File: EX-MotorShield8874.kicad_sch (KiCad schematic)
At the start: 23 parts, among them J101 MC 1,5/ 2-G-3,5, J101 Power, J102 Analog, J103 Digital/PWM, J103 MC 1,5/ 2-G-3,5, J104 Digital/PWM, J105 STEMMA QT, J106 I2C, J107 OLED, J108 USB_B_Micro, J111 JTAG, SW101 FLASH, U101 ESP32-S2-MINI-2, Y101 40Mhz

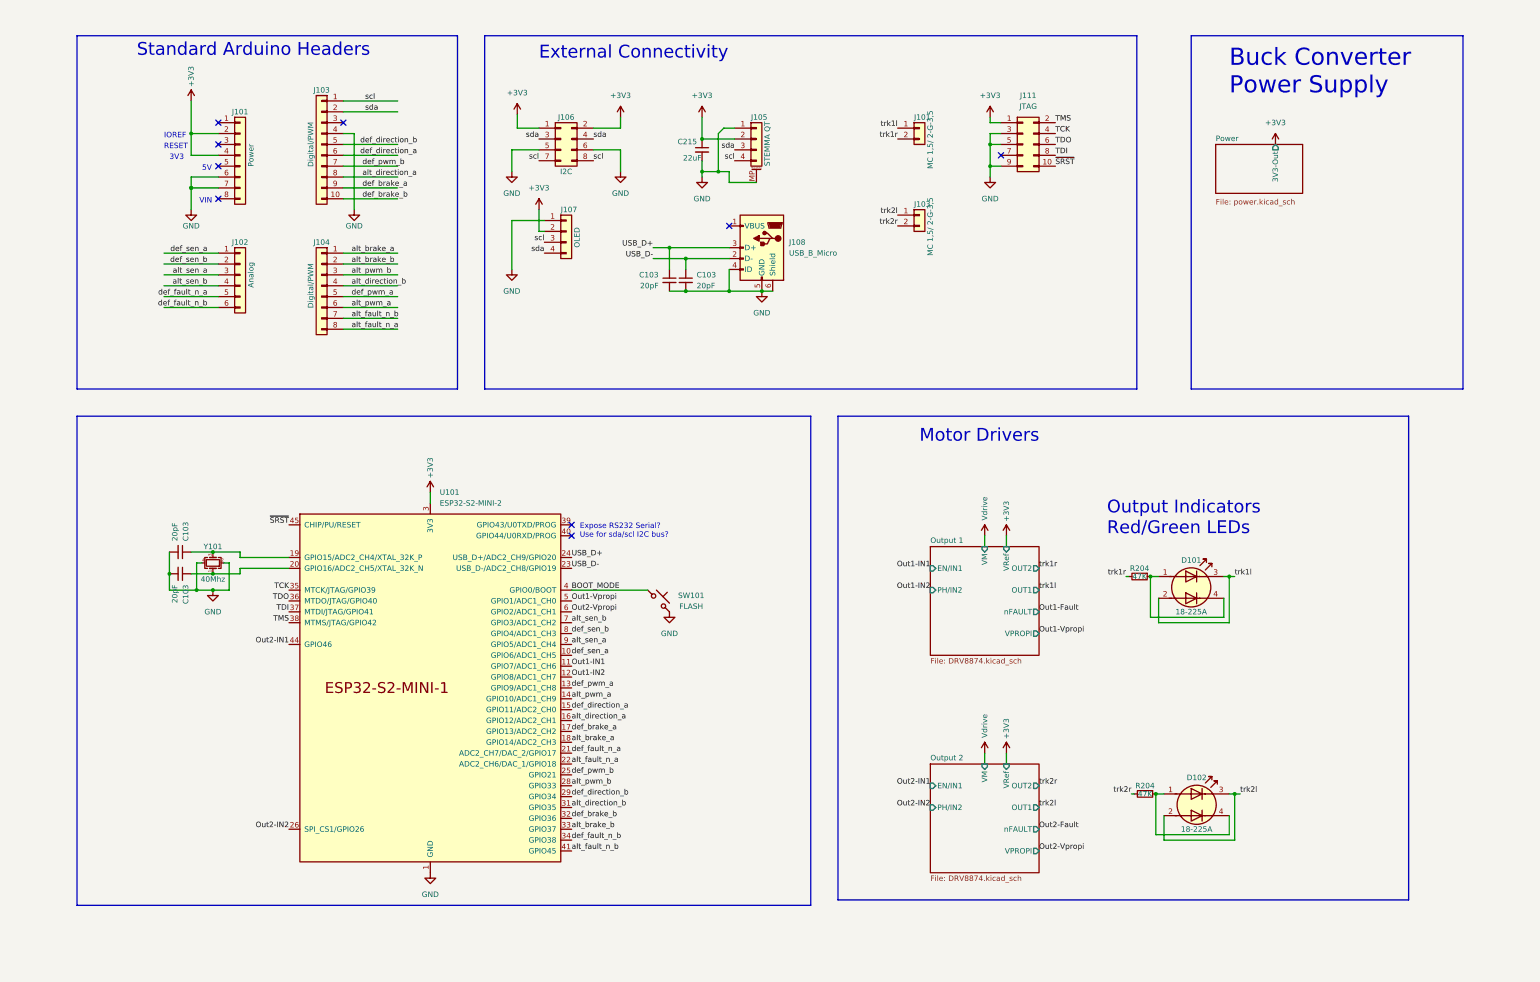
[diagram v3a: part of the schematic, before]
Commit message: Stand alone, purpose build command station doodle.
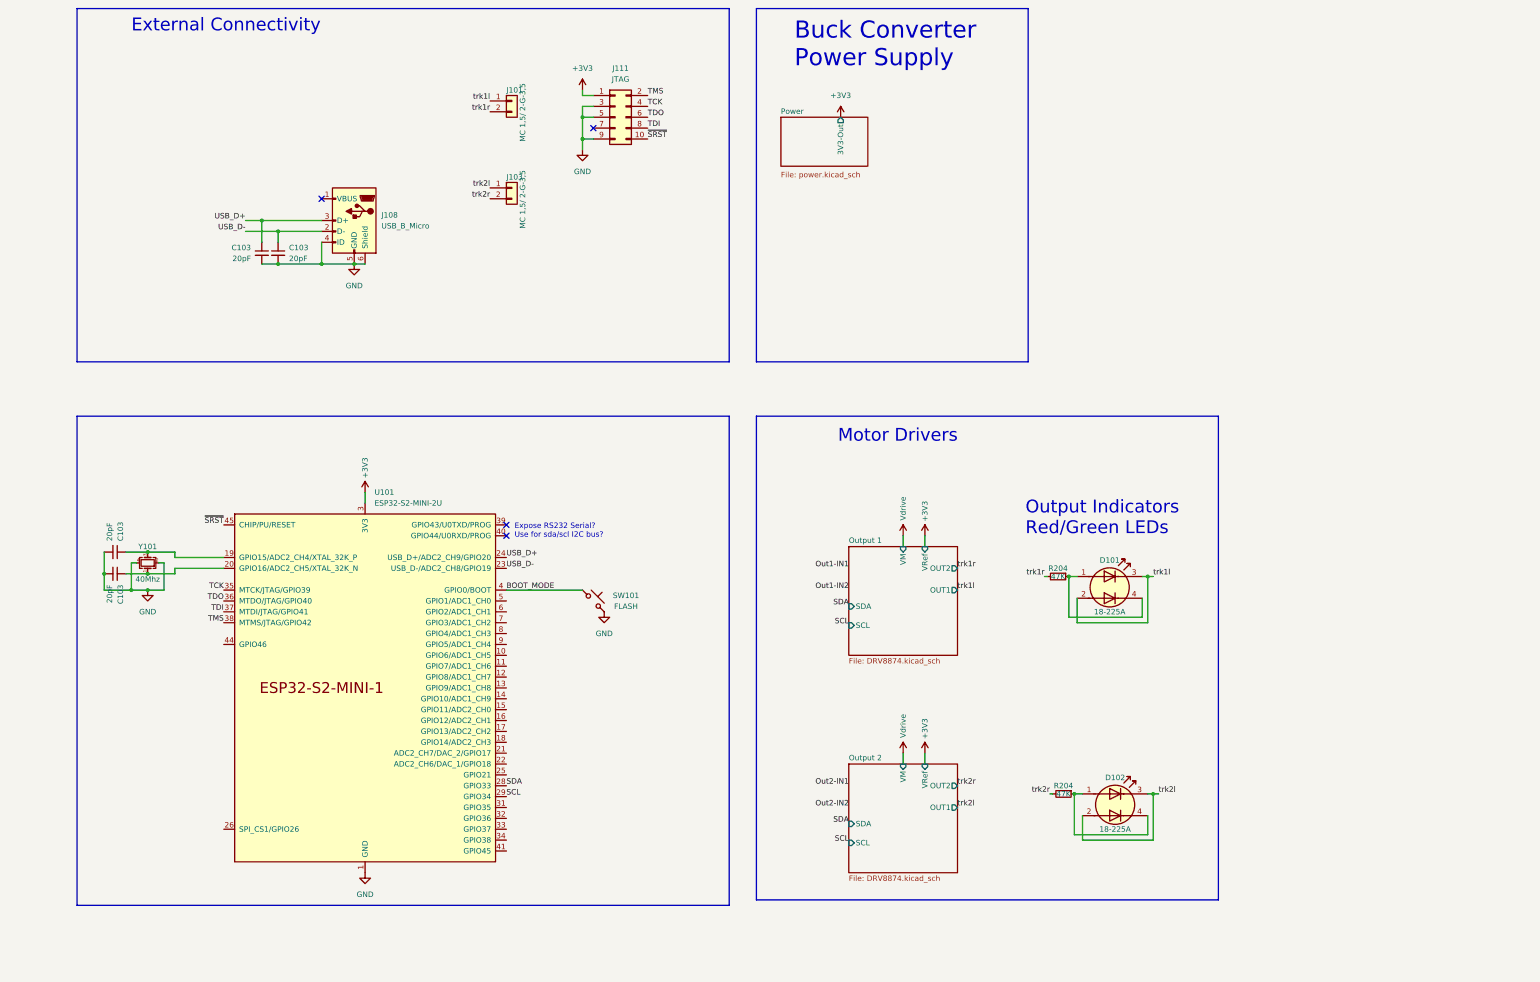
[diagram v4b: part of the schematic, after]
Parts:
- removed C215: 22uF, Capacitor_SMD:C_0805_2012Metric, symbol Device:C_Small
- removed J101: Power, Connector_PinSocket_2.54mm:PinSocket_1x08_P2.54mm_Vertical, symbol Connector_Generic:Conn_01x08
- removed J102: Analog, Connector_PinSocket_2.54mm:PinSocket_1x06_P2.54mm_Vertical, symbol Connector_Generic:Conn_01x06
- removed J103: Digital/PWM, Connector_PinSocket_2.54mm:PinSocket_1x10_P2.54mm_Vertical, symbol Connector_Generic:Conn_01x10
- removed J104: Digital/PWM, Connector_PinSocket_2.54mm:PinSocket_1x08_P2.54mm_Vertical, symbol Connector_Generic:Conn_01x08
- removed J105: STEMMA QT, Connector_JST:JST_SH_SM04B-SRSS-TB_1x04-1MP_P1.00mm_Horizontal, symbol Connector_Generic_MountingPin:Conn_01x04_MountingPin
- removed J106: I2C, Connector_PinHeader_2.54mm:PinHeader_2x04_P2.54mm_Vertical, symbol Connector_Generic:Conn_02x04_Odd_Even
- removed J107: OLED, Connector_PinSocket_2.54mm:PinSocket_1x04_P2.54mm_Vertical, symbol Connector_Generic:Conn_01x04
- U101: value ESP32-S2-MINI-2 -> ESP32-S2-MINI-2U; LCSC Part # C3013906 -> C3013909; MPN ESP32-S2-MINI-2-N4 -> ESP32-S2-MINI-2U-N4R4
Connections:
- net Out1-IN1: no longer U101.11 (GPIO7/ADC1_CH6)
- net Out1-IN2: no longer U101.12 (GPIO8/ADC1_CH7)
- net Out2-IN1: no longer U101.44 (GPIO46)
- net Out2-IN2: no longer U101.26 (SPI_CS1/GPIO26)
- net Out1-Vpropi: no longer names the net of U101.5 (GPIO1/ADC1_CH0)
- net Out2-Vpropi: no longer names the net of U101.6 (GPIO2/ADC1_CH1)
- net alt_brake_a: no longer names the net of U101.18 (GPIO14/ADC2_CH3)
- net alt_brake_b: no longer names the net of U101.33 (GPIO37)
- net alt_direction_a: no longer names the net of U101.16 (GPIO12/ADC2_CH1)
- net alt_direction_b: no longer names the net of U101.31 (GPIO35)
- net alt_fault_n_a: no longer names the net of U101.22 (ADC2_CH6/DAC_1/GPIO18)
- net alt_fault_n_b: no longer names the net of U101.41 (GPIO45)
- net alt_pwm_a: no longer names the net of U101.14 (GPIO10/ADC1_CH9)
- net alt_pwm_b renamed SDA
- net alt_sen_a: no longer names the net of U101.9 (GPIO5/ADC1_CH4)
- net alt_sen_b: no longer names the net of U101.7 (GPIO3/ADC1_CH2)
- net def_brake_a: no longer names the net of U101.17 (GPIO13/ADC2_CH2)
- net def_brake_b: no longer names the net of U101.32 (GPIO36)
- net def_direction_a: no longer names the net of U101.15 (GPIO11/ADC2_CH0)
- net def_direction_b renamed SCL
- net def_fault_n_a: no longer names the net of U101.21 (ADC2_CH7/DAC_2/GPIO17)
- net def_fault_n_b: no longer names the net of U101.34 (GPIO38)
- net def_pwm_a: no longer names the net of U101.13 (GPIO9/ADC1_CH8)
- net def_pwm_b: no longer names the net of U101.25 (GPIO21)
- net def_sen_a: no longer names the net of U101.10 (GPIO6/ADC1_CH5)
- net def_sen_b: no longer names the net of U101.8 (GPIO4/ADC1_CH3)
- no-connect marks 9 -> 4
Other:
- sheet Output 1 ports: added SCL, SDA; removed EN/IN1, PH/IN2, VPROPI, nFAULT
- sheet Output 2 ports: added SCL, SDA; removed EN/IN1, PH/IN2, VPROPI, nFAULT
- note removed: "3V3"
- note removed: "5V"
- note removed: "IOREF"
- note removed: "RESET"
- note removed: "Standard Arduino Headers"
- note removed: "VIN"
- moved on the sheet: C103, D101, D102, J101, J103, J108, J111, R204, SW101, U101, Y101
